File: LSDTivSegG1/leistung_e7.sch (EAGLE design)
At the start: 80 parts, among them IC1 LM 2576 T5,0, IC2 IR2184D, IC3 IR2184D, IC4 4081N, IC5 4069N, IC6 LM 2576 T15, IC7 IR2184D, IC8 IR2184D, IC9 TINY13-20PU, X1 057-010-1, X2 MKDSN1,5/2-5,08

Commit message: eagle 7 export
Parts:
- added C19, C20: 4m7, rcl:CPOL-EUE7.5-18
- added R11, R12, R13, R25: 470k, rcl:R-EU_0207/7
- C1, C11: value 10u -> 4m7; device rcl:CPOL-EUE2.5-5 -> rcl:CPOL-EUE7.5-18
- C6: device rcl@1:CPOL-EUE2.5-5V -> rcl:CPOL-EUE5-13
- C9: device rcl@1:CPOL-EUE5-13 -> rcl:CPOL-EUE5-13
- D1, D13, D14, D2: value 1N4001 -> 1N4002
- D15, D16, D17, D18, D3, D4, D5, D6: value 18 -> ZD-5W_18V
- D7, D8: value 1N 5711 -> 1N5822
- Q1, Q10, Q11, Q12, Q2, Q3, Q4, Q9: value (none) -> IRFB3077
- R10: value (none) -> 20k
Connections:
- removed net BAT_PWM_IN: IC9.PB0/PCINT0/AIN0/OC0A/MOSI
- removed net DIRL_IN_INV: IC5A.O
- removed net DIRR_IN_INV: IC5B.O
- removed net MOTOR_L_ACTIVE: IC2.!SD, IC3.!SD, IC4A.O
- removed net MOTOR_R_ACTIVE: IC4B.O, IC7.!SD, IC8.!SD
- removed net N$15: IC4C.O
- removed net N$16: IC4D.O
- removed net N$21: IC4C.I0
- removed net N$22: IC4C.I1
- removed net N$23: IC4D.I0
- removed net N$24: IC4D.I1
- removed net N$29: D16.C, Q10.G, R18.2, R23.1
- removed net NC2: X1-10.S
- removed net VB: C12.+, C13.+, C2.+, C3.+, D1.C, D13.C, D14.C, D2.C, IC2.VB, IC3.VB, IC7.VB, IC8.VB
- new net IN_L: IC2.IN, IC4B.O
- new net IN_L_INVD: IC3.IN, IC4D.O
- new net IN_R: IC4A.O, IC7.IN
- new net IN_R_INVD: IC4C.O, IC8.IN
- new net N$13: D16.C, Q10.G, R18.2, R23.2
- new net VB1: C2.+, D1.C, IC2.VB
- new net VB2: C3.+, D2.C, IC3.VB
- new net VB3: C12.+, D13.C, IC7.VB
- new net VB4: C13.+, D14.C, IC8.VB
- net +24V: now also X1-10.S
- net BAT_+: now also C19.+, C20.+
- net BAT_PWM: now also IC9.PB0/PCINT0/AIN0/OC0A/MOSI
- net DIRL: now also IC4B.I0, IC5B.I; no longer IC2.IN, IC5A.I
- net DIRL_INV: now also IC4D.I0, IC5B.O; no longer IC3.IN
- net DIRR: now also IC4A.I0, IC5A.I; no longer IC5B.I, IC7.IN
- net DIRR_INV: now also IC4C.I0, IC5A.O; no longer IC8.IN
- net ENABLE: now also IC2.!SD, IC3.!SD, IC7.!SD, IC8.!SD, R11.2, R12.2, R13.2, R25.2; no longer IC4A.I0, IC4B.I0
- net GND: now also C19.-, C20.-, D16.A, D17.A, D4.A, D5.A, R11.1, R12.1, R13.1, R22.1, R23.1, R25.1, R6.1, R7.1
- net MOTOR_L_+: no longer D4.A, R7.2
- net MOTOR_L_-: no longer D5.A, R6.2
- net MOTOR_PWM_L: now also IC4B.I1, IC4D.I1; no longer IC4A.I1
- net MOTOR_PWM_R: now also IC4A.I1, IC4C.I1; no longer IC4B.I1
- net MOTOR_R_+: no longer D16.A, R23.2
- net MOTOR_R_-: no longer D17.A, R22.2
- net N$32: now also R22.2; no longer R22.1
- net N$5: now also R7.2; no longer R7.1
- net N$8: now also R6.2; no longer R6.1
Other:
- note removed: "Mosfets IRFB3077"
- note removed: "_CTL indicates position on LOW-Voltage Side of board"
- moved on the sheet: C1, C11, C6, C9, D16, D17, D4, D5, R18, R19, R2, R22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

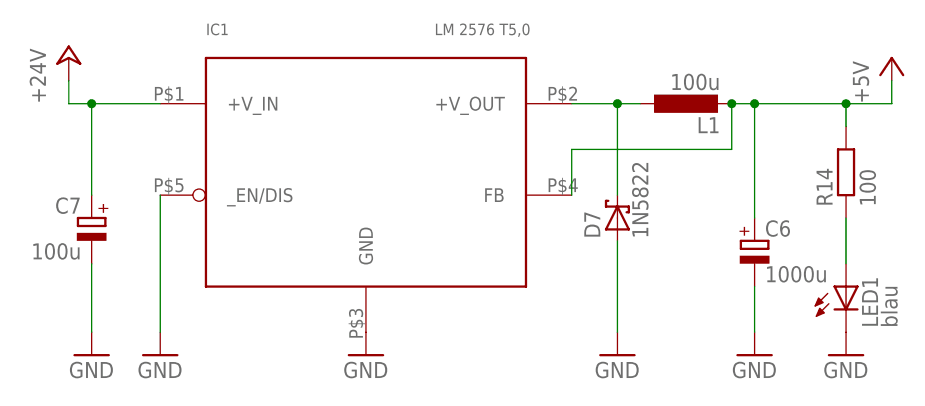
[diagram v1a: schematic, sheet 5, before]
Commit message: updated eagle7 copatible exports of display and leistung boards
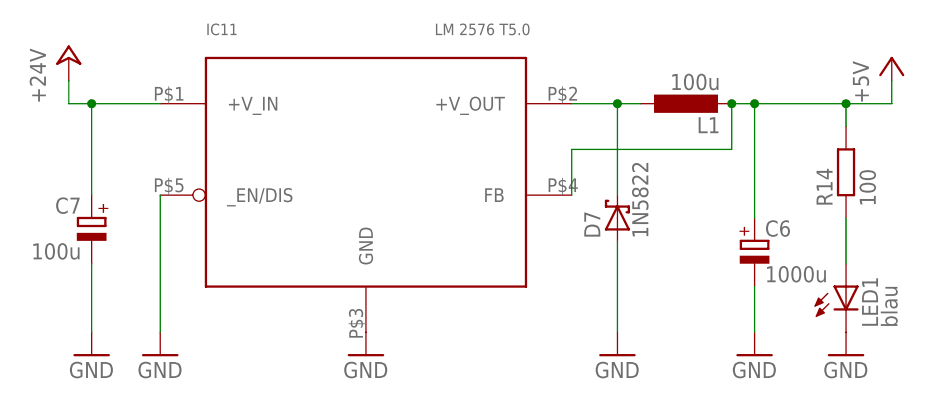
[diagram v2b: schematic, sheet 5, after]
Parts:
- removed IC1: LM 2576 T5,0, LM2576:LM2576-T05A
- removed IC6: LM 2576 T15, LM2576:LM2576-T05A
- added IC10: LM 2576 T15, LM2576:LM2576-T05D
- added IC11: LM 2576 T5.0, LM2576:LM2576-T05D
- F1, F2, F3: value (none) -> 1A
- L1, L2: device rcl@1:L-EU0204/5 -> rcl@1:L-EU0207/10
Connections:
- net +15V: now also IC10.FB; no longer IC6.FB
- net +24V: now also IC10.+V_IN, IC11.+V_IN; no longer IC1.+V_IN, IC6.+V_IN
- net +5V: now also IC11.FB; no longer IC1.FB
- net GND: now also IC10.GND, IC10._EN/DIS, IC11.GND, IC11._EN/DIS; no longer IC1.GND, IC1._EN/DIS, IC6.GND, IC6._EN/DIS
- net N$1: now also IC11.+V_OUT; no longer IC1.+V_OUT
- net N$4: now also IC10.+V_OUT; no longer IC6.+V_OUT
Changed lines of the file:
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@@
 <part name="IC4" library="40xx" deviceset="4081" device="N"/>
 <part name="IC5" library="40xx" deviceset="4069" device="N"/>
-<part name="F1" library="special" deviceset="FUSE" device=""/>
-<part name="F2" library="special" deviceset="FUSE" device=""/>
-<part name="F3" library="special" deviceset="FUSE" device=""/>
+<part name="F1" library="special" deviceset="FUSE" device="" value="1A"/>
+<part name="F2" library="special" deviceset="FUSE" device="" value="1A"/>
+<part name="F3" library="special" deviceset="FUSE" device="" value="1A"/>
 <part name="X2" library="con-phoenix-508" deviceset="MKDSN1,5/2-5,08" device=""/>
 <part name="FRAME5" library="frames" deviceset="DINA4_L" device=""/>
@@
 <part name="P+2" library="hcontrol" deviceset="+5V" device=""/>
 <part name="GND2" library="SparkFun-Aesthetics" deviceset="GND" device=""/>
-<part name="IC1" library="LM2576" deviceset="LM2576-T05A" device="" value="LM 2576 T5,0"/>
-<part name="L1" library="rcl@1" deviceset="L-EU" device="0204/5" value="100u"/>
+<part name="L1" library="rcl@1" deviceset="L-EU" device="0207/10" value="100u"/>
 <part name="GND3" library="supply1" deviceset="GND" device=""/>
 <part name="GND4" library="supply1" deviceset="GND" device=""/>
@@
 <part name="R14" library="rcl@1" deviceset="R-EU_" device="0207/10" value="100"/>
 <part name="FRAME2" library="frames@1" deviceset="FRAME_A_L" device=""/>
-<part name="IC6" library="LM2576" deviceset="LM2576-T05A" device="" value="LM 2576 T15 "/>
 <part name="D8" library="diode@1" deviceset="SCHOTTKY-DIODE" device="CB429-15" value="1N5822"/>
 <part name="C8" library="rcl@1" deviceset="CPOL-EU" device="E2.5-7" value="100u"/>
-<part name="L2" library="rcl@1" deviceset="L-EU" device="0204/5" value="100u"/>
+<part name="L2" library="rcl@1" deviceset="L-EU" device="0207/10" value="100u"/>
 <part name="GND7" library="supply1" deviceset="GND" device=""/>
 <part name="GND8" library="supply1" deviceset="GND" device=""/>
@@
 <part name="C9" library="rcl" deviceset="CPOL-EU" device="E5-13" value="1000u"/>
 <part name="C6" library="rcl" deviceset="CPOL-EU" device="E5-13" value="1000u"/>
+<part name="IC10" library="LM2576" deviceset="LM2576-T05D" device="" value="LM 2576 T15"/>
+<part name="IC11" library="LM2576" deviceset="LM2576-T05D" device="" value="LM 2576 T5.0"/>
 </parts>
 <sheets>
@@
 </plain>
 <instances>
-<instance part="IC1" gate="G$1" x="119.38" y="106.68"/>
 <instance part="L1" gate="G$1" x="154.94" y="114.3" rot="R90"/>
 <instance part="GND3" gate="1" x="119.38" y="86.36"/>
@@
 <instance part="FRAME2" gate="G$2" x="172.72" y="0"/>
 <instance part="C6" gate="G$1" x="162.56" y="99.06"/>
+<instance part="IC11" gate="G$1" x="119.38" y="106.68"/>
 </instances>
 <busses>
@@
 <net name="GND" class="0">
 <segment>
-<pinref part="IC1" gate="G$1" pin="GND"/>
-<pinref part="GND3" gate="1" pin="GND"/>
-</segment>
-<segment>
 <pinref part="GND5" gate="1" pin="GND"/>
 <pinref part="D7" gate="G$1" pin="A"/>
@@
 <segment>
 <pinref part="GND10" gate="1" pin="GND"/>
-<pinref part="IC1" gate="G$1" pin="_EN/DIS"/>
 <wire x1="96.52" y1="88.9" x2="96.52" y2="104.14" width="0.1524" layer="91"/>
+<pinref part="IC11" gate="G$1" pin="_EN/DIS"/>
 </segment>
 <segment>
@@
 <wire x1="162.56" y1="93.98" x2="162.56" y2="88.9" width="0.1524" layer="91"/>
 </segment>
+<segment>
+<pinref part="GND3" gate="1" pin="GND"/>
+<pinref part="IC11" gate="G$1" pin="GND"/>
+</segment>
 </net>
 <net name="+24V" class="0">
@@
 <pinref part="P+3" gate="1" pin="+24V"/>
 <wire x1="86.36" y1="116.84" x2="86.36" y2="114.3" width="0.1524" layer="91"/>
-<pinref part="IC1" gate="G$1" pin="+V_IN"/>
 <wire x1="86.36" y1="114.3" x2="88.9" y2="114.3" width="0.1524" layer="91"/>
 <pinref part="C7" gate="G$1" pin="+"/>
@@
 <wire x1="88.9" y1="104.14" x2="88.9" y2="114.3" width="0.1524" layer="91"/>
 <junction x="88.9" y="114.3"/>
+<pinref part="IC11" gate="G$1" pin="+V_IN"/>
 </segment>
 </net>
@@
 <wire x1="172.72" y1="114.3" x2="172.72" y2="111.76" width="0.1524" layer="91"/>
 <junction x="172.72" y="114.3"/>
-<pinref part="IC1" gate="G$1" pin="FB"/>
 <wire x1="142.24" y1="104.14" x2="142.24" y2="109.22" width="0.1524" layer="91"/>
 <wire x1="142.24" y1="109.22" x2="160.02" y2="109.22" width="0.1524" layer="91"/>
@@
 <wire x1="162.56" y1="101.6" x2="162.56" y2="114.3" width="0.1524" layer="91"/>
 <junction x="162.56" y="114.3"/>
+<pinref part="IC11" gate="G$1" pin="FB"/>
 </segment>
 </net>
 <net name="N$1" class="0">
 <segment>
-<pinref part="IC1" gate="G$1" pin="+V_OUT"/>
 <pinref part="L1" gate="G$1" pin="1"/>
 <wire x1="142.24" y1="114.3" x2="147.32" y2="114.3" width="0.1524" layer="91"/>
@@
 <wire x1="147.32" y1="104.14" x2="147.32" y2="114.3" width="0.1524" layer="91"/>
 <junction x="147.32" y="114.3"/>
+<pinref part="IC11" gate="G$1" pin="+V_OUT"/>
 </segment>
 </net>
@@
 </plain>
 <instances>
-<instance part="IC6" gate="G$1" x="114.3" y="109.22"/>
 <instance part="D8" gate="G$1" x="144.78" y="104.14" rot="R90"/>
 <instance part="C8" gate="G$1" x="83.82" y="104.14"/>
@@
 <instance part="FRAME6" gate="G$2" x="172.72" y="0"/>
 <instance part="C9" gate="G$1" x="160.02" y="101.6"/>
+<instance part="IC10" gate="G$1" x="114.3" y="109.22"/>
 </instances>
 <busses>
@@
 </segment>
 <segment>
-<pinref part="IC6" gate="G$1" pin="GND"/>
-<pinref part="GND11" gate="1" pin="GND"/>
-</segment>
-<segment>
 <pinref part="GND8" gate="1" pin="GND"/>
 <pinref part="C9" gate="G$1" pin="-"/>
@@
 </segment>
 <segment>
-<pinref part="IC6" gate="G$1" pin="_EN/DIS"/>
 <pinref part="GND12" gate="1" pin="GND"/>
 <wire x1="91.44" y1="106.68" x2="91.44" y2="91.44" width="0.1524" layer="91"/>
+<pinref part="IC10" gate="G$1" pin="_EN/DIS"/>
 </segment>
 <segment>
@@
 <wire x1="170.18" y1="91.44" x2="170.18" y2="93.98" width="0.1524" layer="91"/>
 </segment>
+<segment>
+<pinref part="GND11" gate="1" pin="GND"/>
+<pinref part="IC10" gate="G$1" pin="GND"/>
+</segment>
 </net>
 <net name="+24V" class="0">
@@
 <pinref part="P+5" gate="1" pin="+24V"/>
 <wire x1="81.28" y1="116.84" x2="81.28" y2="119.38" width="0.1524" layer="91"/>
-<pinref part="IC6" gate="G$1" pin="+V_IN"/>
 <wire x1="81.28" y1="116.84" x2="83.82" y2="116.84" width="0.1524" layer="91"/>
 <pinref part="C8" gate="G$1" pin="+"/>
@@
 <wire x1="83.82" y1="106.68" x2="83.82" y2="116.84" width="0.1524" layer="91"/>
 <junction x="83.82" y="116.84"/>
+<pinref part="IC10" gate="G$1" pin="+V_IN"/>
 </segment>
 </net>
@@
 <wire x1="160.02" y1="116.84" x2="160.02" y2="109.22" width="0.1524" layer="91"/>
 <junction x="160.02" y="116.84"/>
-<pinref part="IC6" gate="G$1" pin="FB"/>
 <wire x1="137.16" y1="106.68" x2="137.16" y2="111.76" width="0.1524" layer="91"/>
 <wire x1="137.16" y1="111.76" x2="157.48" y2="111.76" width="0.1524" layer="91"/>
@@
 <wire x1="160.02" y1="104.14" x2="160.02" y2="106.68" width="0.1524" layer="91"/>
 <wire x1="160.02" y1="106.68" x2="160.02" y2="109.22" width="0.1524" layer="91"/>
+<pinref part="IC10" gate="G$1" pin="FB"/>
 </segment>
 </net>
 <net name="N$4" class="0">
 <segment>
-<pinref part="IC6" gate="G$1" pin="+V_OUT"/>
 <wire x1="137.16" y1="116.84" x2="144.78" y2="116.84" width="0.1524" layer="91"/>
 <pinref part="D8" gate="G$1" pin="C"/>
@@
 <wire x1="144.78" y1="116.84" x2="147.32" y2="116.84" width="0.1524" layer="91"/>
 <junction x="144.78" y="116.84"/>
-</segment>
-</net>
+<pinref part="IC10" gate="G$1" pin="+V_OUT"/>
+</segment>
+</net>
